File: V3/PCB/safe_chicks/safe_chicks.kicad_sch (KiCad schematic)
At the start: 58 parts, among them J1 5V, J2 PGM, J3 Serial, J4 Buttons, J5 MOTOR, J6 Sensors, J8 Switches, J9 LED-Enable, SW1 Reset, U1 PIC18F2550-ISP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

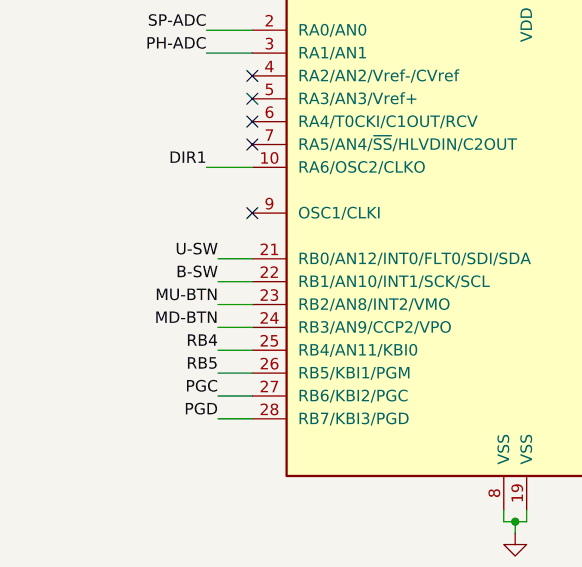
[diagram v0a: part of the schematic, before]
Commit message: Move button pins so they can be used for interrupts
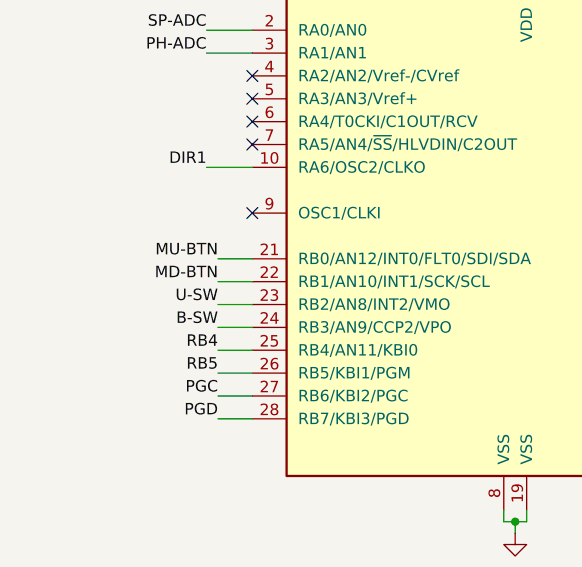
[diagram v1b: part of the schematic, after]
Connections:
- net B-SW: now also U1.24 (RB3/AN9/CCP2/VPO); no longer U1.22 (RB1/AN10/INT1/SCK/SCL)
- net MD-BTN: now also U1.22 (RB1/AN10/INT1/SCK/SCL); no longer U1.24 (RB3/AN9/CCP2/VPO)
- net MU-BTN: now also U1.21 (RB0/AN12/INT0/FLT0/SDI/SDA); no longer U1.23 (RB2/AN8/INT2/VMO)
- net U-SW: now also U1.23 (RB2/AN8/INT2/VMO); no longer U1.21 (RB0/AN12/INT0/FLT0/SDI/SDA)
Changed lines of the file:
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@@
 	)
 	(label "MD-BTN"
-		(at 39.37 76.2 180)
+		(at 39.37 71.12 180)
 		(effects
 			(font
@@
 	)
 	(label "U-SW"
-		(at 39.37 68.58 180)
+		(at 39.37 73.66 180)
 		(effects
 			(font
@@
 	)
 	(label "MU-BTN"
-		(at 39.37 73.66 180)
+		(at 39.37 68.58 180)
 		(effects
 			(font
@@
 	)
 	(label "B-SW"
-		(at 39.37 71.12 180)
-		(effects
-			(font
+		(at 39.37 76.2 180)
+		(effects
+			(font
